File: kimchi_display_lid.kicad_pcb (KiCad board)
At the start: 4 copper layers, 147 x 77 mm, 36 parts, among them J1 DF40HC(3.5)-60DS, J2 DF40HC(3.5)-60DS, J3 H19C-6S-0.5SH, J4 FH19C-40S-0.5SH(10), J5 USB_A, U1 24C32, U2 AP3019AKTR-G1, U3 TXS0108EPW, U4 LSM9DS1

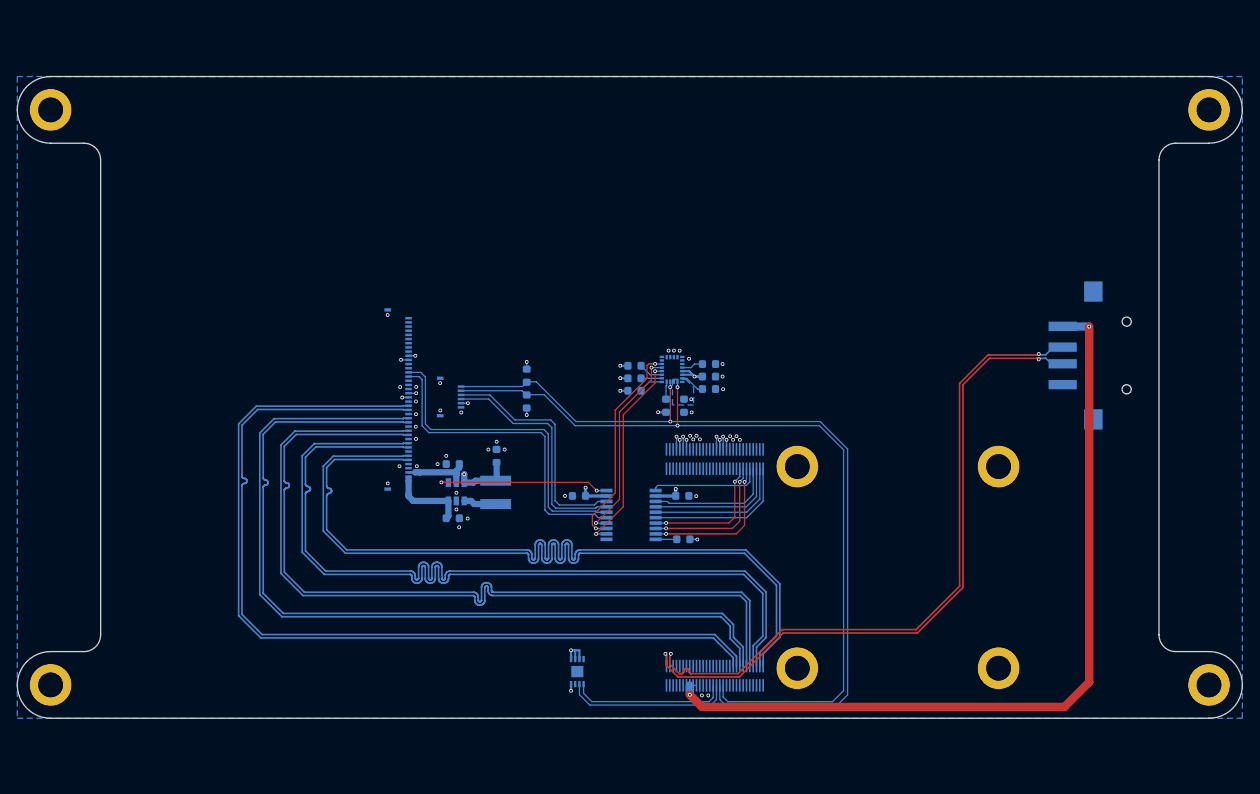
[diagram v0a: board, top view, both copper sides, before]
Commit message: Add ESD protection and filtering to USB and DSI
Signed-off-by: Michael Welling <mwelling@ieee.org>
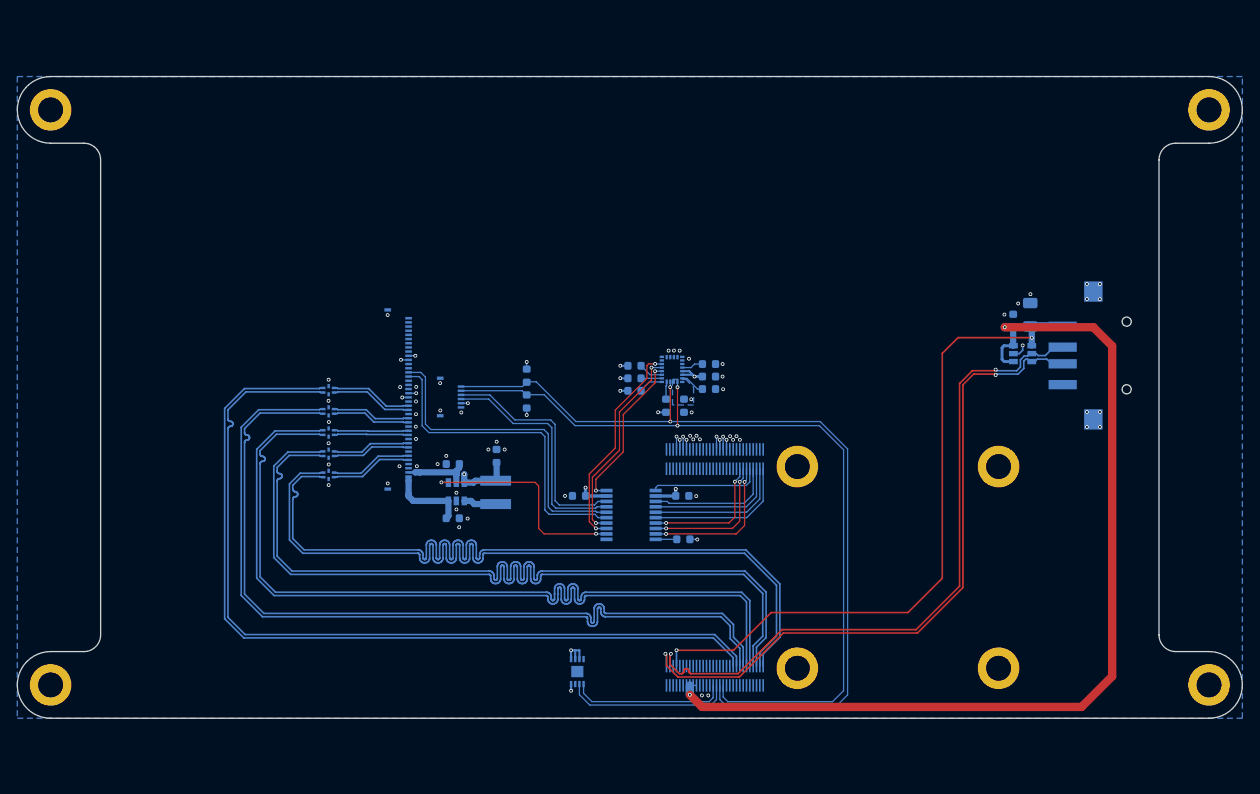
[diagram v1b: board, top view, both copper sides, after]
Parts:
- added C10: .1uF, Capacitor_SMD:C_0603_1608Metric, B.Cu at (184.5, 98.3)
- added C9: 100uF, Capacitor_SMD:C_1206_3216Metric, B.Cu at (186.6, 97.6)
- added L2: LCFE121002, kimchi_ulid:LCFE121002, B.Cu at (102.4, 106.6)
- added L3: LCFE121002, kimchi_ulid:LCFE121002, B.Cu at (102.4, 109.2)
- added L4: LCFE121002, kimchi_ulid:LCFE121002, B.Cu at (102.4, 111.7)
- added L5: LCFE121002, kimchi_ulid:LCFE121002, B.Cu at (102.4, 114.3)
- added L6: LCFE121002, kimchi_ulid:LCFE121002, B.Cu at (102.4, 116.8)
- added U5: TPD3S014, Package_TO_SOT_SMD:SOT-23-6, B.Cu at (185.6, 102.2)
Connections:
- J1 pad 57: USB2_VBUS -> VBUS
- J1 pad 58: USB2_ID -> GND
- J4 pad 10: /DISP_D1_P -> /DISP1_D1_P
- J4 pad 12: /DISP_CK_N -> /DISP1_CK_N
- J4 pad 13: /DISP_CK_P -> /DISP1_CK_P
- J4 pad 15: /DISP_D2_N -> /DISP1_D2_N
- J4 pad 16: /DISP_D2_P -> /DISP1_D2_P
- J4 pad 18: /DISP_D3_N -> /DISP1_D3_N
- J4 pad 19: /DISP_D3_P -> /DISP1_D3_P
- J4 pad 6: /DISP_D0_N -> /DISP1_D0_N
- J4 pad 7: /DISP_D0_P -> /DISP1_D0_P
- J4 pad 9: /DISP_D1_N -> /DISP1_D1_N
- J5 pad 1: VDD_5V -> VBUS
- U3 pad 12: /DRDY_M -> /BL_PWM
- U3 pad 20: /BL_PWM -> /DRDY_M
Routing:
- net VBUS: track 0.00 -> 82.2 mm, vias 0 -> 2
- net VDD_5V: track 97.9 -> 116.2 mm
- net /DISP1_D3_P: track 0.00 -> 9.89 mm
- net /DISP1_D3_N: track 0.00 -> 9.89 mm
- net /DISP1_D0_N: track 0.00 -> 9.87 mm
- net /DISP1_D0_P: track 0.00 -> 9.87 mm
- net /DISP1_D2_N: track 0.00 -> 9.46 mm
- net /DISP1_D2_P: track 0.00 -> 9.46 mm
- net /DISP1_D1_P: track 0.00 -> 9.44 mm
- net /DISP1_D1_N: track 0.00 -> 9.44 mm
- net /DISP1_CK_P: track 0.00 -> 9.03 mm
- net /DISP1_CK_N: track 0.00 -> 9.03 mm
- net /DRDY_M: track 24.5 -> 19.3 mm
- net /BL_PWM: track 21.1 -> 26.2 mm
- net /DISP_D3_N: track 106.8 -> 102.1 mm
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
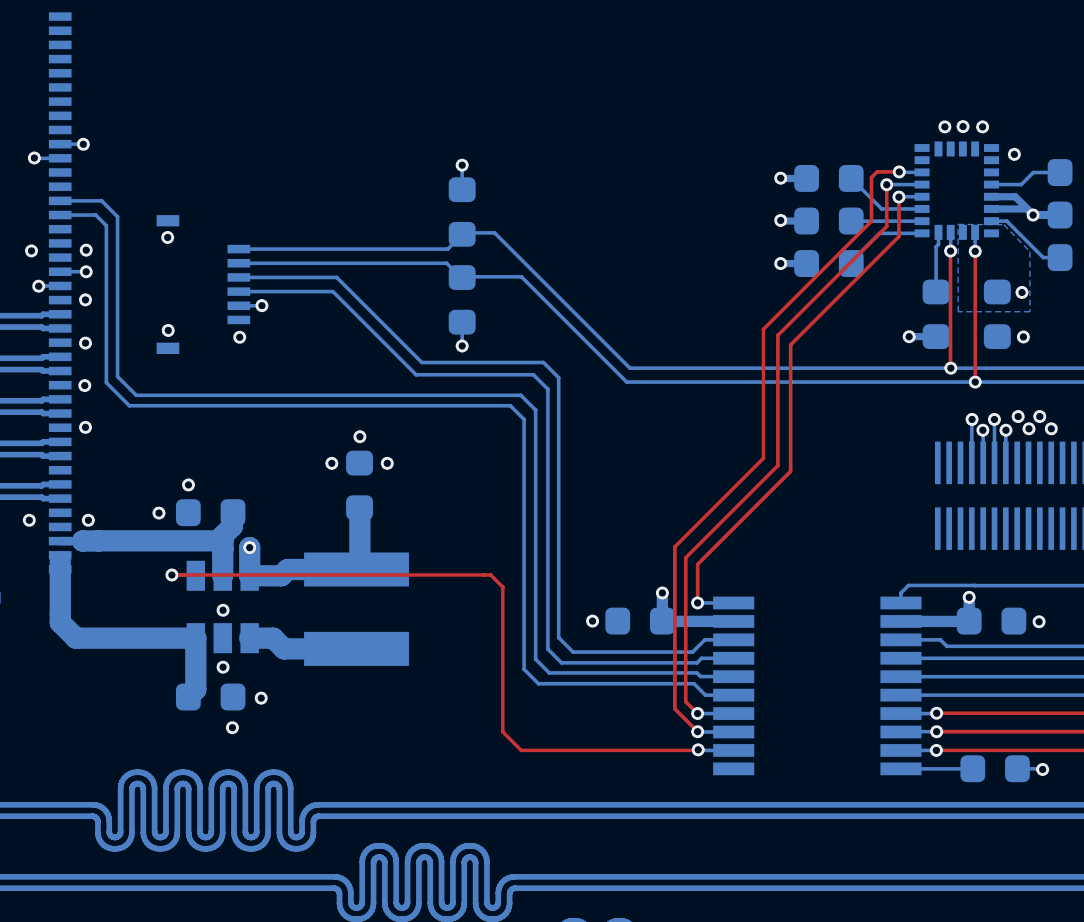
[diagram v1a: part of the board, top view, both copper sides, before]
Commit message: Whooops PWM is on GPIO1_13
Signed-off-by: Michael Welling <mwelling@ieee.org>
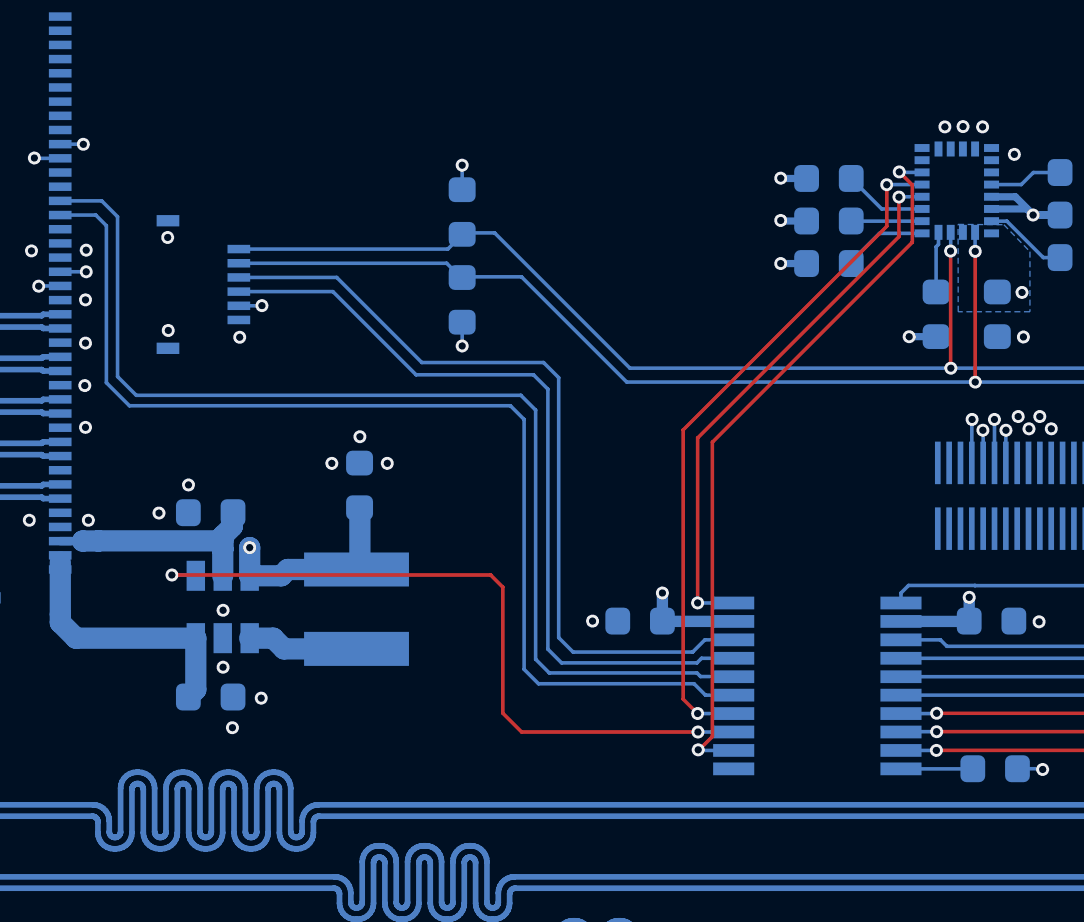
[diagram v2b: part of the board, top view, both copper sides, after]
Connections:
- U3 pad 12: /BL_PWM -> /INT1A_G
- U3 pad 13: /INT1A_G -> /BL_PWM
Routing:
- net /BL_PWM: track 26.2 -> 25.6 mm

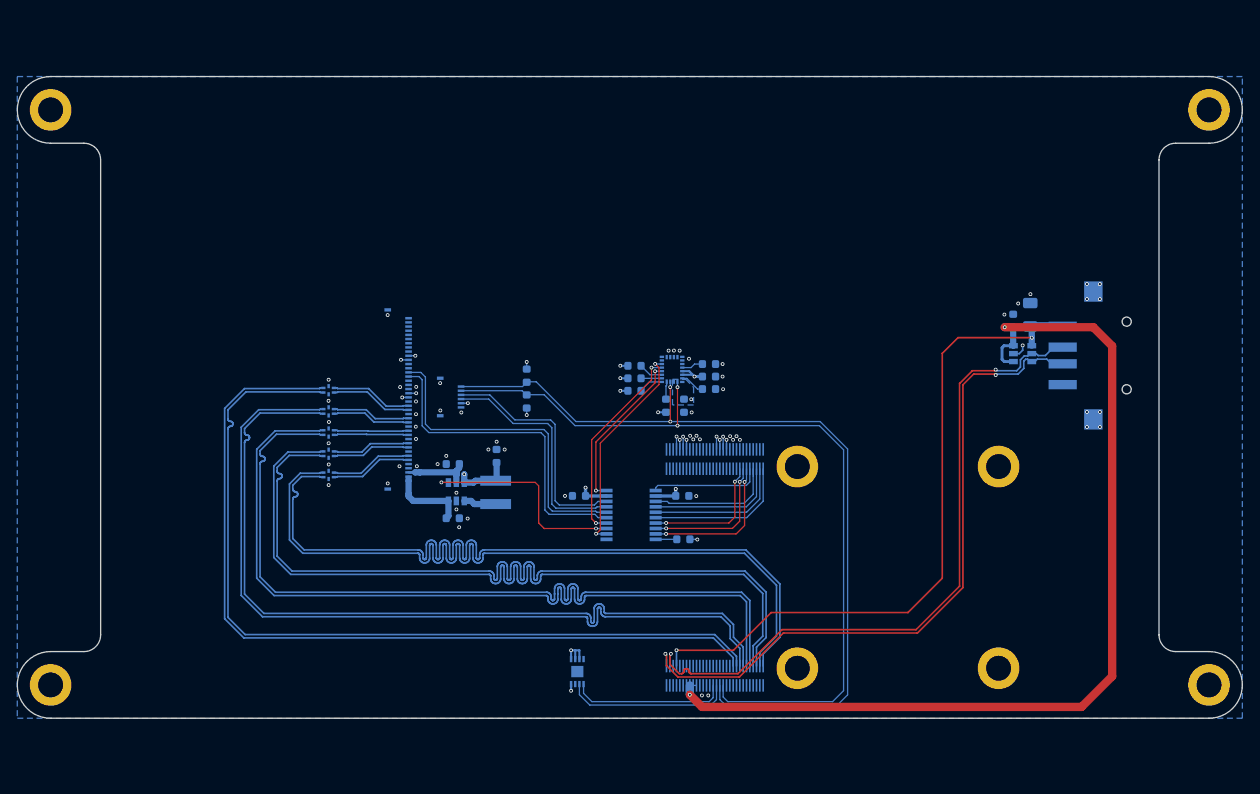
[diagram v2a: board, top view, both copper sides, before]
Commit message: Move the mounting holes to avoid blocking LCD FPC
Also removes a bit length on the board to compensate for
the cable wrapping around the PCB.

May have to move the touchsreen connector and use an adapter
to add length.

Signed-off-by: Michael Welling <mwelling@ieee.org>
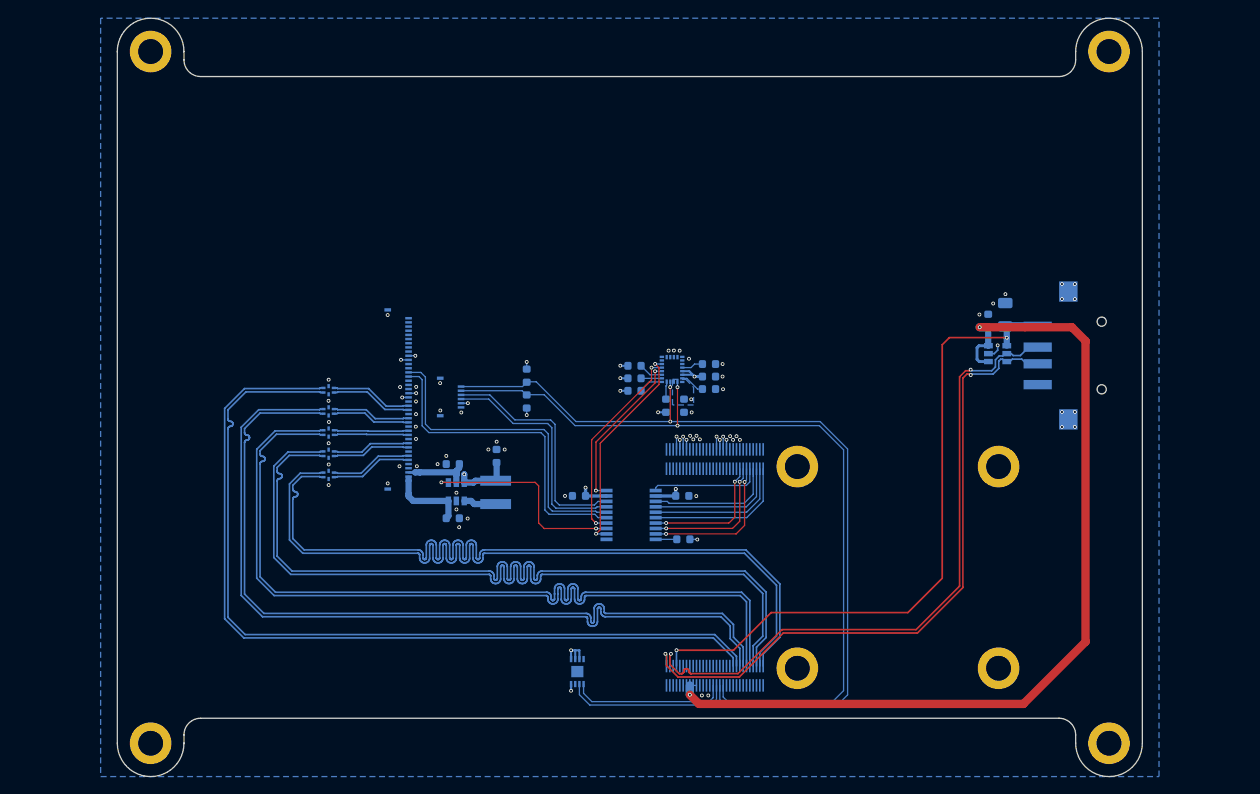
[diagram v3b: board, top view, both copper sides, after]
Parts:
- moved H5 13.9 mm to (81.0, 149.0)
- moved H6 13.9 mm to (81.0, 66.0)
- moved H7 13.9 mm to (196.0, 66.0)
- moved H8 13.9 mm to (196.0, 149.0)
- moved C10 3.00 mm to (181.5, 98.3)
- moved C9 3.00 mm to (183.6, 97.6)
- moved J5 3.00 mm to (195.1, 102.5)
- moved U5 3.00 mm to (182.6, 102.2)
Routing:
- net VDD_5V: track 116.2 -> 110.4 mm
- net USB2_DN: track 82.4 -> 79.9 mm
- net USB2_DP: track 82.2 -> 79.7 mm
- net VBUS: track 82.2 -> 79.8 mm
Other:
- board size 147 x 77 mm -> 123 x 91 mm

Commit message: Add part numbers to the schematic for BOM export
Signed-off-by: Michael Welling <mwelling@ieee.org>
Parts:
- moved LOGO1 74.3 mm to (123.8, 141.0)
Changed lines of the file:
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@@
   (page A)
   (title_block
-    (title kimchi_ulid)
-    (date 2019-12-15)
+    (title kimchi_display_lid)
+    (date 2021-01-12)
     (rev v0.1)
     (company GroupGets)
@@
   )
   (module Symbol:OSHW-Logo_5.7x6mm_SilkScreen (layer B.Cu)
-    (at 198.15 142.1 180)
+    (at 123.83 141.04 180)
     (descr "Open Source Hardware Logo")
     (tags "Logo OSHW")

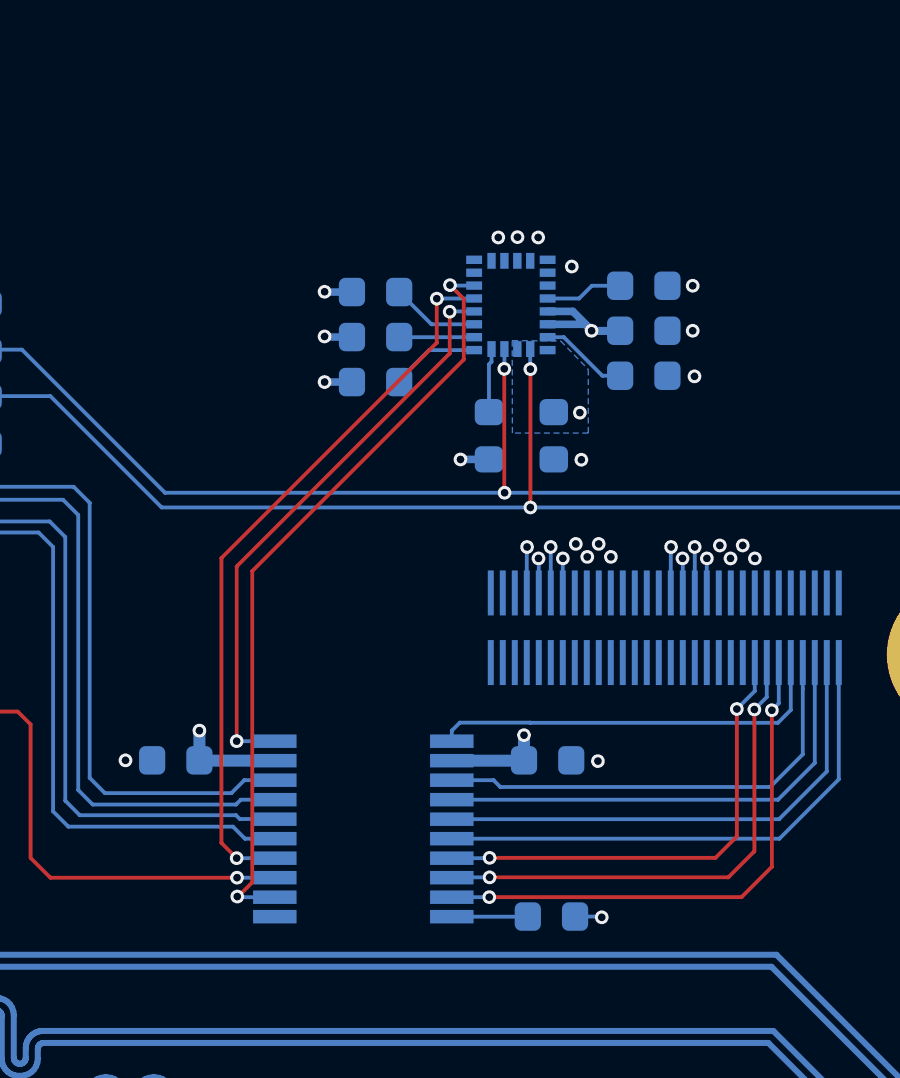
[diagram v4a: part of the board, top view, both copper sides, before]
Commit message: IMU Changed
9DOF IMU is out of stock, added new IMU that is 6DOF adjusted PCB design to include new IMU.
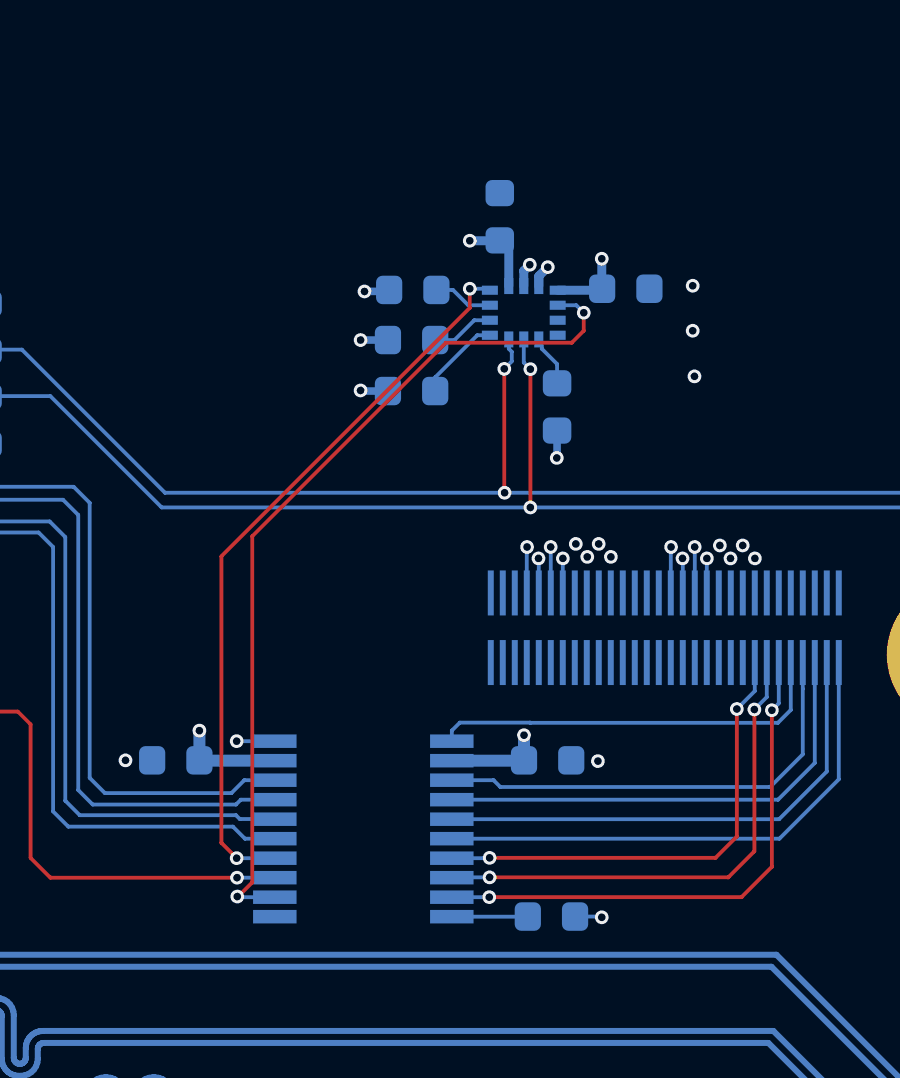
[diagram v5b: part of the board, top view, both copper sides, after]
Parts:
- removed C5: 10uF, Capacitor_SMD:C_0603_1608Metric
- removed C6: .1uF, Capacitor_SMD:C_0603_1608Metric
- U4: value LSM9DS1 -> LSM6DSRTR; footprint kimchi_ulid:PQFN24P43_350X300X102L35X23N -> kimchi_ulid:LSM6DSRTR
- moved C7 7.52 mm to (143.2, 101.2), turned to 90 degrees
- moved R8 7.16 mm to (145.1, 107.5), turned to 270 degrees
- moved R6 5.48 mm to (140.3, 103.6), turned to 0 degrees
- moved R7 2.16 mm to (140.3, 107.0)
- moved R5 1.84 mm to (140.3, 105.3)
- moved C8 1.52 mm to (147.4, 103.6)
- moved U4 0.50 mm to (144.0, 104.4), turned to 0 degrees
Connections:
- U4 pad 1: VDD_3V3 -> Net-(R7-Pad1)
- U4 pad 10: /INT_M -> Net-(U4-Pad10)
- U4 pad 11: /INT1A_G -> Net-(U4-Pad11)
- U4 pad 12: Net-(U4-Pad12) -> Net-(R8-Pad1)
- U4 pad 13: Net-(U4-Pad13) -> I2C3_SCL
- U4 pad 14: GND -> I2C3_SDA
- U4 pad 2: I2C3_SCL -> Net-(R5-Pad2)
- U4 pad 3: VDD_3V3 -> Net-(R6-Pad2)
- U4 pad 4: I2C3_SDA -> /INT_M
- U4 pad 5: Net-(R6-Pad2) -> VDD_3V3
- U4 pad 6: Net-(R5-Pad2) -> GND
- U4 pad 7: Net-(R7-Pad1) -> GND
- U4 pad 8: Net-(R8-Pad1) -> VDD_3V3
- U4 pad 9: /DRDY_M -> /INT1A_G
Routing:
- net /DRDY_M: track 19.3 -> 1.27 mm, vias 2 -> 1
- net /INT1A_G: track 25.8 -> 29.0 mm
- net Net-(C5-Pad1): track 2.95 -> 0.00 mm
- net Net-(C6-Pad1): track 2.59 -> 0.00 mm
- net GND: track 1.86 -> 3.41 mm, vias 60 -> 57
- net Net-(R8-Pad1): track 2.94 -> 1.72 mm
- net Net-(R5-Pad2): track 2.98 -> 2.16 mm
- removed copper zone on B.Cu, net VDD_3V3

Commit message: Logos
added logots
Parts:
- added L7: GG_LOGO, kimchi_ulid:groupgets_logo, B.Cu at (108.4, 141.0)
- added L8: OSHPARK_LOGO, kimchi_ulid:oshpark_logo, B.Cu at (116.8, 140.6)
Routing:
- net GND: vias 57 -> 58
